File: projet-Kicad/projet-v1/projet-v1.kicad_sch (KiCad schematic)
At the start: 5 parts, among them J1 Power, J2 Digital/PWM, J3 Analog, J4 Digital/PWM

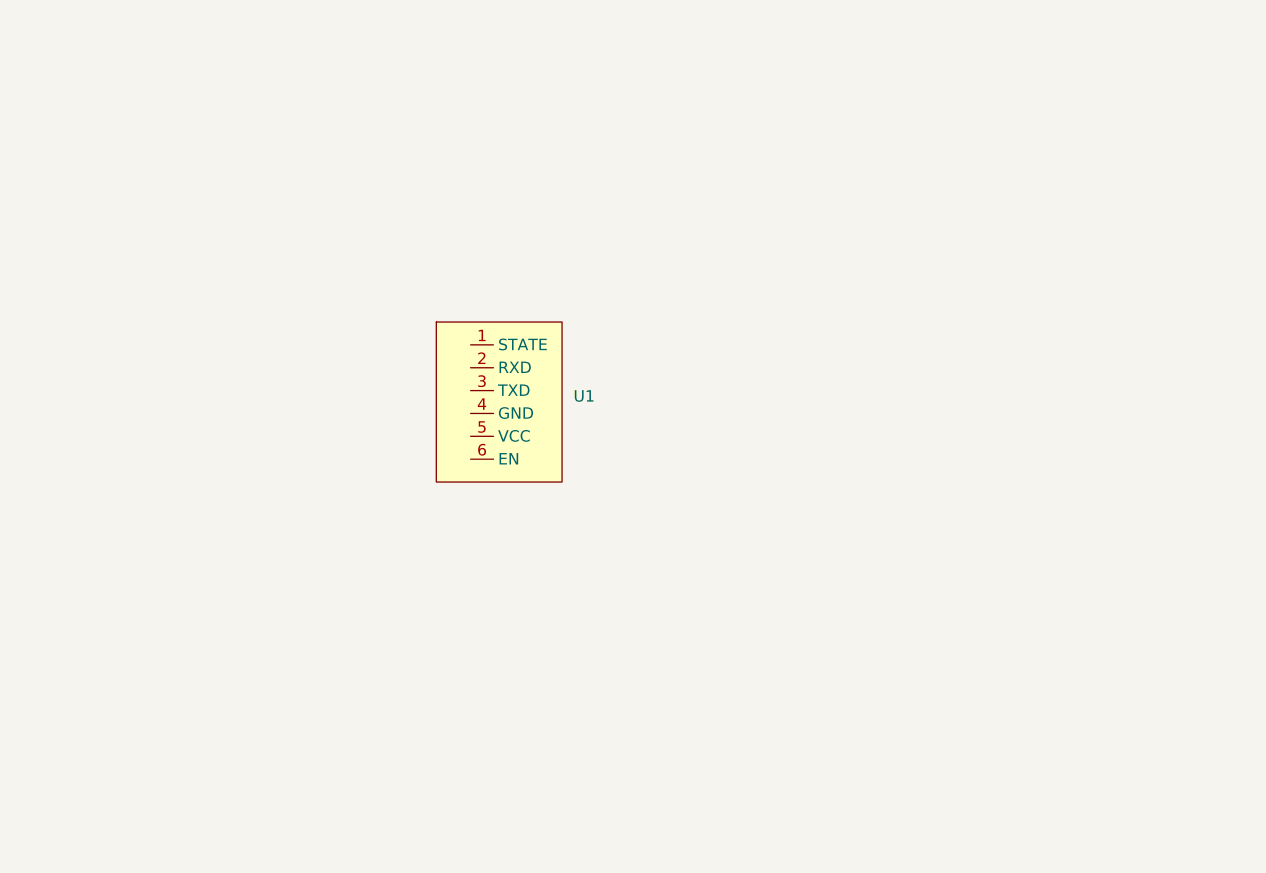
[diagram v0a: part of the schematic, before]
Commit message: Ajout des resistances et des capa dans la schematique
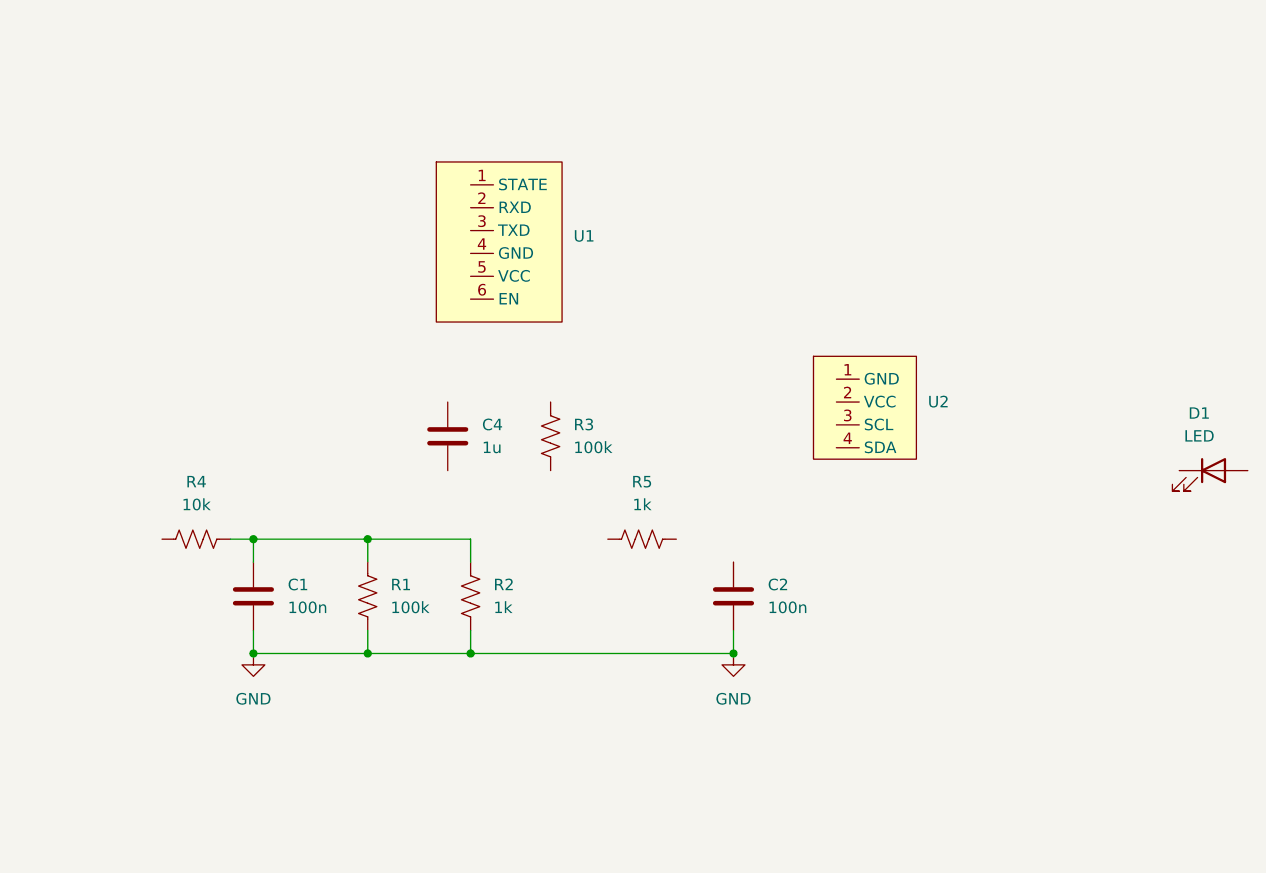
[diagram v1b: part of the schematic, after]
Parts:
- added C1, C2: 100n, Capacitor_THT:C_Disc_D3.0mm_W1.6mm_P2.50mm, symbol Device:C
- added C4: 1u, Capacitor_THT:C_Disc_D3.0mm_W1.6mm_P2.50mm, symbol Device:C
- added D1: LED, LED_THT:LED_D3.0mm, symbol librairie-symboles:LED
- added R1, R3: 100k, Resistor_THT:R_Axial_DIN0207_L6.3mm_D2.5mm_P5.08mm_Vertical, symbol librairie-symboles:R_US
- added R2, R5: 1k, Resistor_THT:R_Axial_DIN0207_L6.3mm_D2.5mm_P5.08mm_Vertical, symbol librairie-symboles:R_US
- added R4: 10k, Resistor_THT:R_Axial_DIN0207_L6.3mm_D2.5mm_P5.08mm_Vertical, symbol librairie-symboles:R_US
- added U2: ~, librairie-empreintes:OLED01, symbol librairie-symboles:OLED01
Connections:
- net GND: now also C1.2, C2.2, R1.2, R2.2
- new net: C1.1, R1.1, R2.1, R4.2
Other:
- moved on the sheet: U1

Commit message: MAJ projet Kicad version envoyée à Cathy
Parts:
- removed D1: LED, LED_THT:LED_D3.0mm, symbol librairie-symboles:LED
- removed R2: 1k, Resistor_THT:R_Axial_DIN0207_L6.3mm_D2.5mm_P5.08mm_Vertical, symbol librairie-symboles:R_US
- added C5: 100n, Capacitor_THT:C_Disc_D4.7mm_W2.5mm_P5.00mm, symbol Device:C
- added R6: 47k, Resistor_THT:R_Axial_DIN0207_L6.3mm_D2.5mm_P5.08mm_Vertical, symbol librairie-symboles:R_US
- added U3: ~, librairie-empreintes:graphite-sensor, symbol librairie-symboles:graphite-sensor
- added U4: ~, librairie-empreintes:MCP41050, symbol librairie-symboles:MCP41050
- added U5: ~, librairie-empreintes:flex-sensor, symbol librairie-symboles:flex-sensor
- added U6: ~, librairie-empreintes:KY-040, symbol librairie-symboles:KY-040
- added U7: ~, librairie-empreintes:LTC1050, symbol librairie-symboles:LTC1050
- C1, C2: footprint Capacitor_THT:C_Disc_D3.0mm_W1.6mm_P2.50mm -> Capacitor_THT:C_Disc_D4.7mm_W2.5mm_P5.00mm
- C4: footprint Capacitor_THT:C_Disc_D3.0mm_W1.6mm_P2.50mm -> Capacitor_THT:C_Rect_L7.0mm_W4.5mm_P5.00mm
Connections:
- net *9 is gone; now on net RXD: J2.9 (Pin_9)
- net 8 is gone; now on net TXD: J2.10 (Pin_10)
- net A0 is gone; now on net ADC: J3.1 (Pin_1)
- net SCL/A5 is gone; now on net SCL: J2.1 (Pin_1), J3.6 (Pin_6)
- net SDA/A4 is gone; now on net SDA: J2.2 (Pin_2), J3.5 (Pin_5)
- net +5V: now also U1.5 (VCC), U2.2 (VCC), U3.1, U4.8 (VDD), U5.1, U6.4 (+), U7.7 (V+)
- net GND: now also U1.4 (GND), U2.1 (GND), C5.2, R6.1, U4.4 (VSS), U4.7 (P0B), U6.5 (GND), U7.4 (V-)
- net at C1.1, R1.1, R4.2: now also U7.3 (+)
- net SCL: now reaches U2.3 (SCL)
- net SDA: now reaches U2.4 (SDA)
- net R2: now reaches R3.1
- net R2: now also C4.1, U4.5 (P0A), U4.6 (P0W), U7.2 (-)
- net at R3.2: now also C4.2, R5.1, U7.6 (OUT)
- net at R4.1: now also U3.2
- net ADC: now reaches C2.1
- net ADC: now also R5.2
- net RXD: now reaches U1.2 (RXD)
- net TXD: now reaches U1.3 (TXD)
- net *10 renamed CS
- net CS: now also U4.1 (CS)
- net *11 renamed SDI
- net SDI: now also U4.3 (SDI/SDO)
- net *3 renamed DT
- net DT: now also U6.2 (DT)
- net 13 renamed SCK
- net SCK: now also U4.2 (SCK)
- net 2 renamed CLK
- net CLK: now also C5.1, U6.1 (CLK)
- net 4 renamed SW
- net SW: now also U6.3 (SW)
- net A1 renamed FS
- net FS: now also R6.2, U5.2
- no-connect marks 1 -> 12
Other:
- moved on the sheet: C1, C2, C4, J1, J2, J3, J4, R1, R3, R4, R5
